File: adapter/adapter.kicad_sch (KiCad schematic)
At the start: 9 parts, among them J10 Ribbon, J11 Ribbon, J12 Ribbon, J9 Ribbon, U1 nice_nano

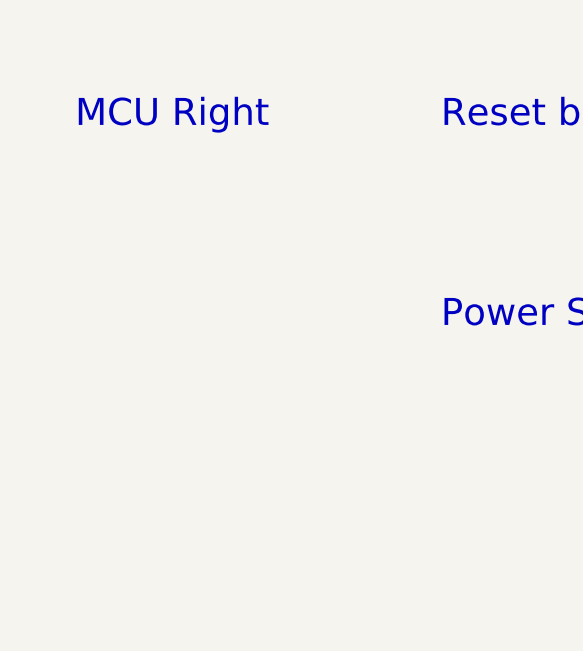
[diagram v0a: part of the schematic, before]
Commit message: Add nice!nano mcu to right side
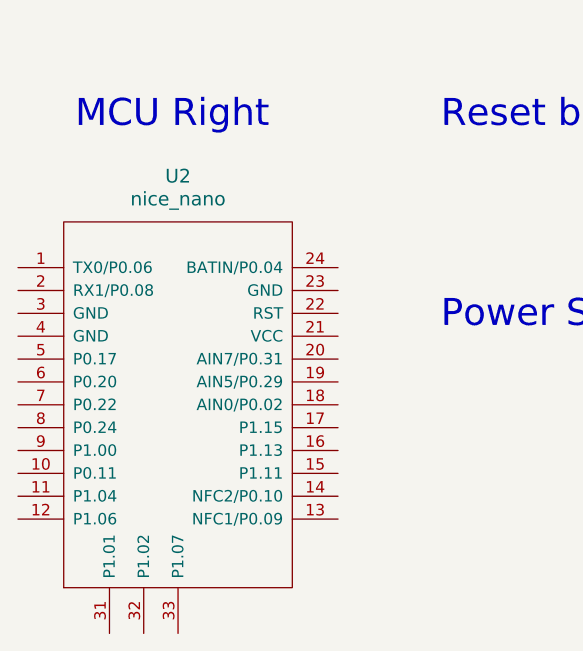
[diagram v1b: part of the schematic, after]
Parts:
- added U2: nice_nano, Library:nice_nano, symbol nice_nano:nice_nano
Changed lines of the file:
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@@
+	)
+	(symbol
+		(lib_id "nice_nano:nice_nano")
+		(at 45.72 129.54 0)
+		(unit 1)
+		(exclude_from_sim no)
+		(in_bom yes)
+		(on_board yes)
+		(dnp no)
+		(fields_autoplaced yes)
+		(property "Reference" "U2"
+			(at 45.72 105.41 0)
+			(effects
+				(font
+					(size 1.524 1.524)
+				)
+			)
+		)
+		(property "Value" "nice_nano"
+			(at 45.72 107.95 0)
+			(effects
+				(font
+					(size 1.524 1.524)
+				)
+			)
+		)
+		(property "Footprint" "Library:nice_nano"
+			(at 72.39 193.04 90)
+			(effects
+				(font
+					(size 1.524 1.524)
+				)
+				(hide yes)
+			)
+		)
+		(property "Datasheet" ""
+			(at 72.39 193.04 90)
+			(effects
+				(font
+					(size 1.524 1.524)
+				)
+				(hide yes)
+			)
+		)
+		(property "Description" ""
+			(at 45.72 129.54 0)
+			(effects
+				(font
+					(size 1.27 1.27)
+				)
+				(hide yes)
+			)
+		)
+		(pin "7"
+		)
+		(pin "1"
+		)
+		(pin "10"
+		)
+		(pin "6"
+		)
+		(pin "5"
+		)
+		(pin "2"
+		)
+		(pin "3"
+		)
+		(pin "4"
+		)
+		(pin "8"
+		)
+		(pin "9"
+		)
+		(pin "12"
+		)
+		(pin "33"
+		)
+		(pin "19"
+		)
+		(pin "16"
+		)
+		(pin "20"
+		)
+		(pin "24"
+		)
+		(pin "15"
+		)
+		(pin "11"
+		)
+		(pin "14"
+		)
+		(pin "17"
+		)
+		(pin "18"
+		)
+		(pin "21"
+		)
+		(pin "23"
+		)
+		(pin "22"
+		)
+		(pin "13"
+		)
+		(pin "31"
+		)
+		(pin "32"
+		)
+		(instances
+			(project ""
+				(path "/e63e39d7-6ac0-4ffd-8aa3-1841a4541b55"
+					(reference "U2")
+					(unit 1)
+				)
+			)
+		)
 	)
 	(symbol

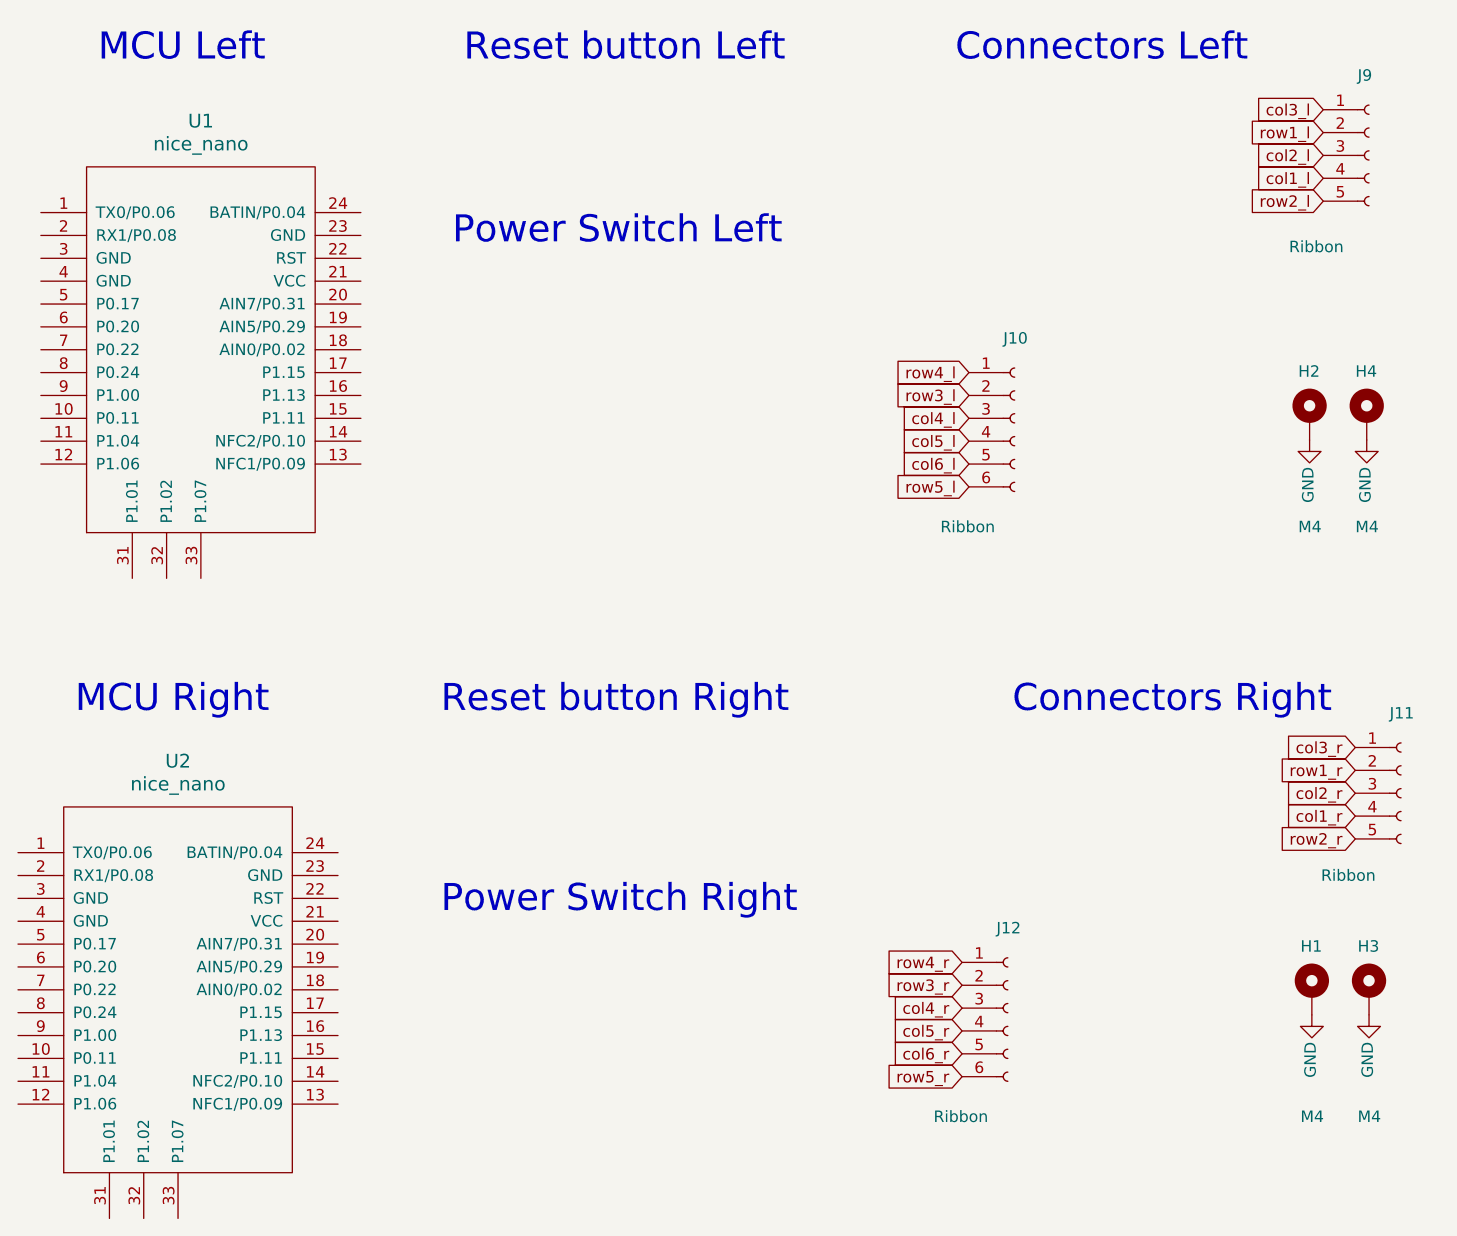
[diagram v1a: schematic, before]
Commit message: Add jst connector and powerswitch
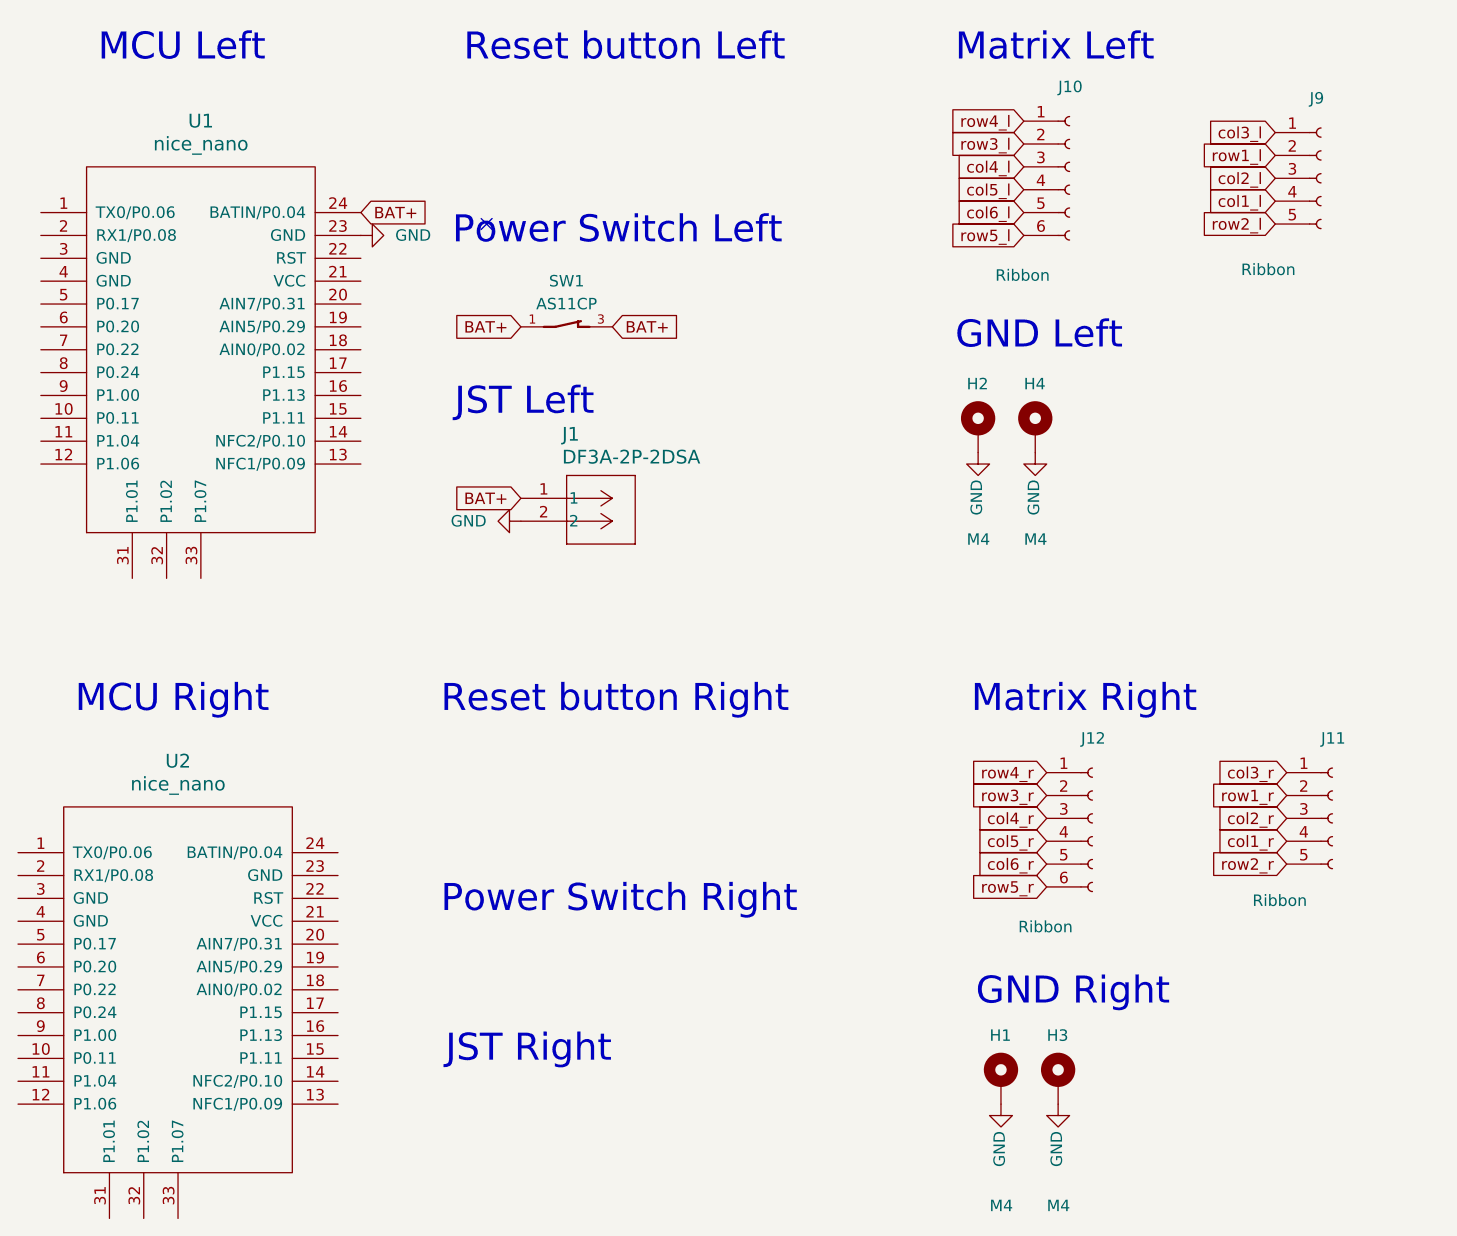
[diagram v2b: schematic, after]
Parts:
- added J1: DF3A-2P-2DSA, Library:DF3A_2P_2DSA, symbol DF3A_2P_2DSA:DF3A-2P-2DSA
- added SW1: AS11CP, Library:SW_AS11CP, symbol AS11CP:AS11CP
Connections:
- net GND: now also U1.23 (GND), J1.2
- net BAT+: now reaches U1.24 (BATIN/P0.04)
- net BAT+: now also J1.1, SW1.1, SW1.3
- no-connect marks 0 -> 1
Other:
- note added: "GND Left"
- note added: "GND Right"
- note added: "JST Left"
- note added: "JST Right"
- note added: "Matrix Left"
- note added: "Matrix Right"
- note removed: "Connectors Left"
- note removed: "Connectors Right"
- moved on the sheet: H1, H2, H3, H4, J10, J11, J12, J9

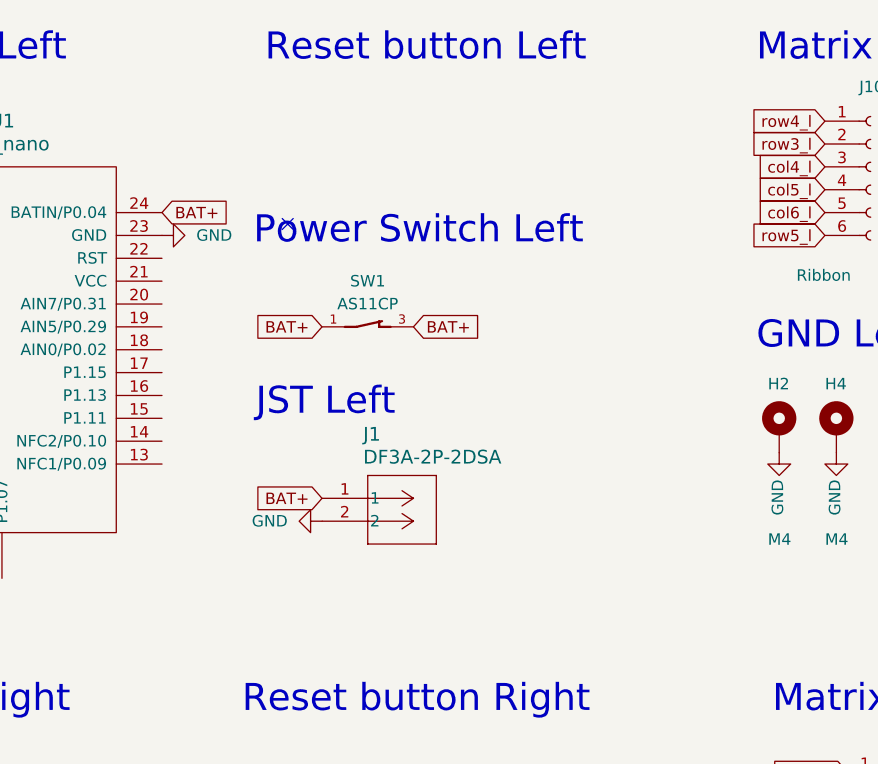
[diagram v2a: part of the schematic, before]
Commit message: Add a resetbutton
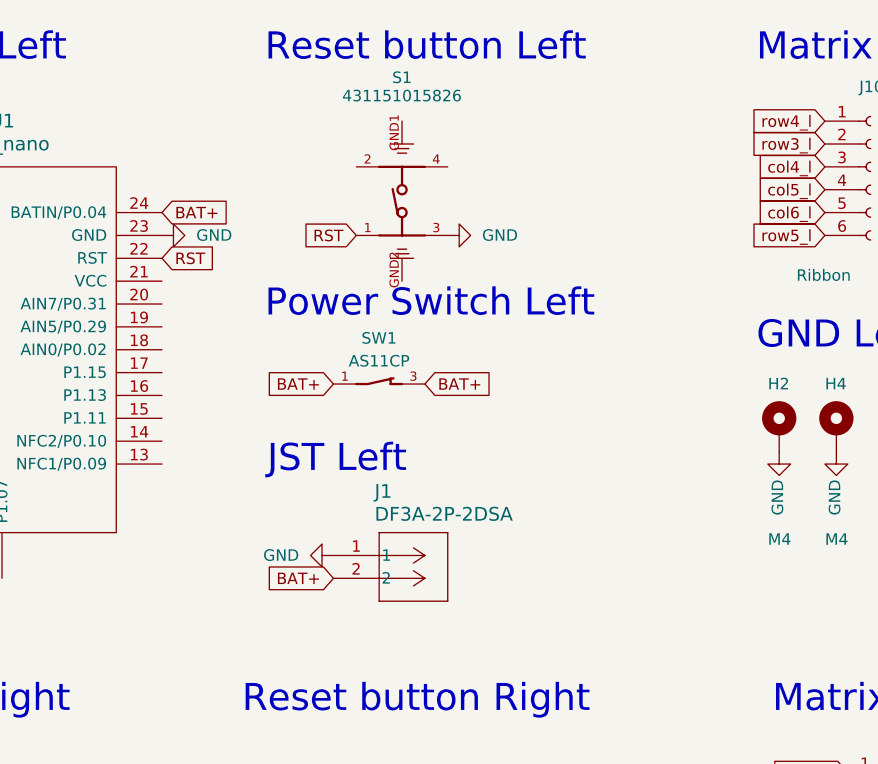
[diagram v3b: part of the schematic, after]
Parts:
- added S1: 431151015826, Library:431151015826, symbol 431151015826:431151015826
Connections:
- net BAT+: now also J1.2; no longer J1.1
- net GND: now also J1.1, S1.3; no longer J1.2
- net RST: now reaches U1.22 (RST)
- net RST: now also S1.1
- no-connect marks 1 -> 0
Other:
- moved on the sheet: J1, SW1

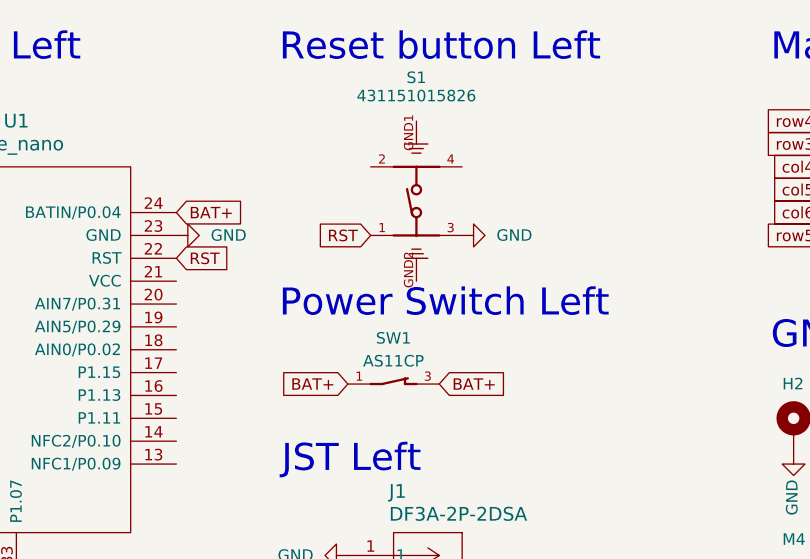
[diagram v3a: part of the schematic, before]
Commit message: Remove power switch
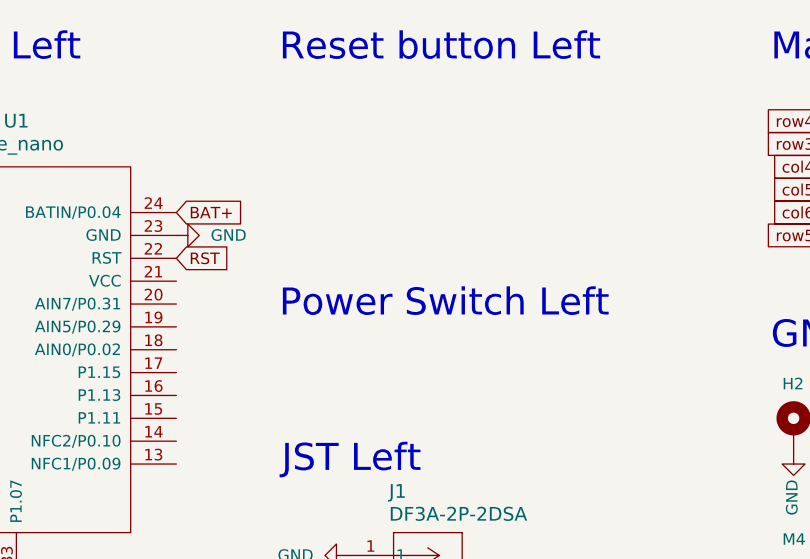
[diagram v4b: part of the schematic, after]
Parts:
- removed S1: 431151015826, Library:431151015826, symbol 431151015826:431151015826
- removed SW1: AS11CP, Library:SW_AS11CP, symbol AS11CP:AS11CP

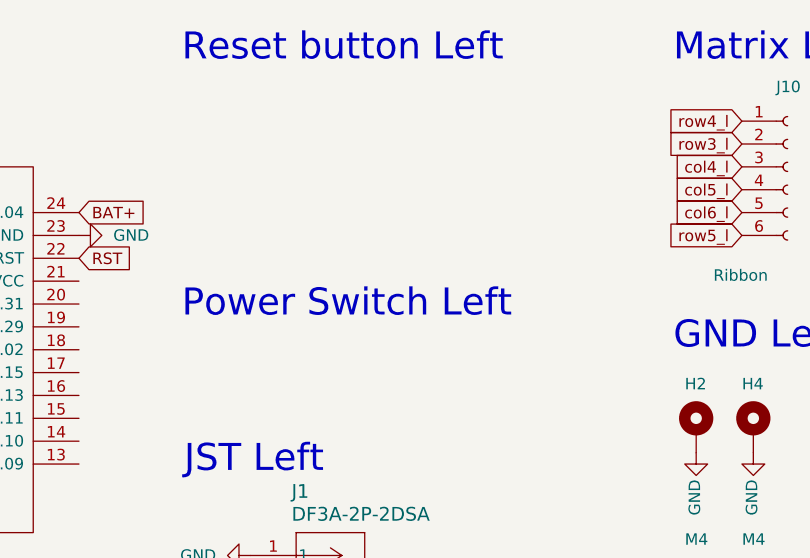
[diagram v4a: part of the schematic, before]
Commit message: Add new power switch and reset button
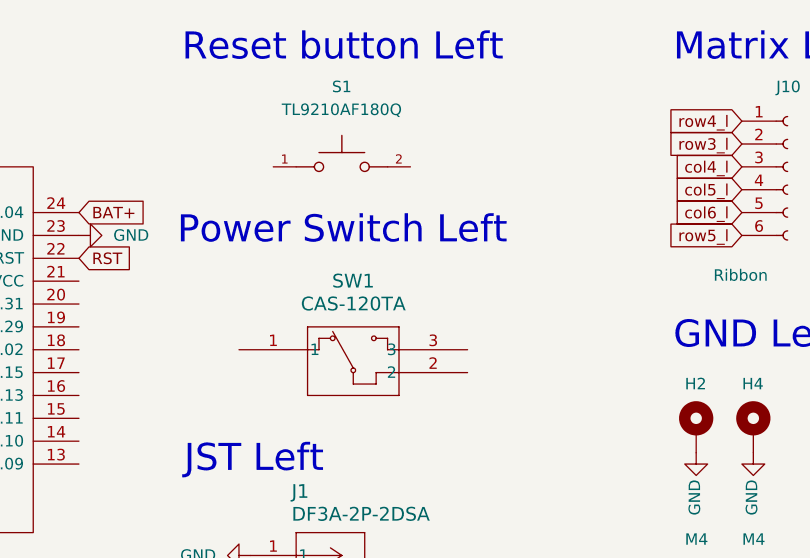
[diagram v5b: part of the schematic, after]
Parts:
- added S1: TL9210AF180Q, Library:SW_TL9210AF180Q, symbol TL9210AF180Q:TL9210AF180Q
- added SW1: CAS-120TA, Library:CAS-120A_NDC, symbol CAS-120TA:CAS-120TA
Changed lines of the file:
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@@
 	(text "Power Switch Left"
 		(exclude_from_sim no)
-		(at 77.47 56.388 0)
+		(at 76.962 48.26 0)
 		(effects
 			(font
@@
 	)
 	(symbol
+		(lib_id "CAS-120TA:CAS-120TA")
+		(at 83.82 59.69 0)
+		(unit 1)
+		(exclude_from_sim no)
+		(in_bom yes)
+		(on_board yes)
+		(dnp no)
+		(fields_autoplaced yes)
+		(property "Reference" "SW1"
+			(at 96.52 52.07 0)
+			(effects
+				(font
+					(size 1.524 1.524)
+				)
+			)
+		)
+		(property "Value" "CAS-120TA"
+			(at 96.52 54.61 0)
+			(effects
+				(font
+					(size 1.524 1.524)
+				)
+			)
+		)
+		(property "Footprint" "Library:CAS-120A_NDC"
+			(at 83.82 59.69 0)
+			(effects
+				(font
+					(size 1.27 1.27)
+					(italic yes)
+				)
+				(hide yes)
+			)
+		)
+		(property "Datasheet" "CAS-120TA"
+			(at 83.82 59.69 0)
+			(effects
+				(font
+					(size 1.27 1.27)
+					(italic yes)
+				)
+				(hide yes)
+			)
+		)
+		(property "Description" ""
+			(at 83.82 59.69 0)
+			(effects
+				(font
+					(size 1.27 1.27)
+				)
+				(hide yes)
+			)
+		)
+		(pin "1"
+		)
+		(pin "3"
+		)
+		(pin "2"
+		)
+		(instances
+			(project ""
+				(path "/e63e39d7-6ac0-4ffd-8aa3-1841a4541b55"
+					(reference "SW1")
+					(unit 1)
+				)
+			)
+		)
+	)
+	(symbol
 		(lib_id "nice_nano:nice_nano")
 		(at 48.26 58.42 0)
@@
 					(unit 1)
 				)
+			)
+		)
+	)
+	(symbol
+		(lib_id "TL9210AF180Q:TL9210AF180Q")
+		(at 95.25 39.37 0)
+		(unit 1)
+		(exclude_from_sim no)
+		(in_bom yes)
+		(on_board yes)
+		(dnp no)
+		(fields_autoplaced yes)
+		(property "Reference" "S1"
+			(at 95.25 30.48 0)
+			(effects
+				(font
+					(size 1.27 1.27)
+				)
+			)
+		)
+		(property "Value" "TL9210AF180Q"
+			(at 95.25 33.02 0)
+			(effects
+				(font
+					(size 1.27 1.27)
+				)
+			)
+		)
+		(property "Footprint" "Library:SW_TL9210AF180Q"
+			(at 95.25 39.37 0)
+			(effects
+				(font
+					(size 1.27 1.27)
+				)
+				(justify bottom)
+				(hide yes)
+			)
+		)
+		(property "Datasheet" ""
+			(at 95.25 39.37 0)
+			(effects
+				(font
+					(size 1.27 1.27)
+				)
+				(hide yes)
+			)
+		)
+		(property "Description" ""
+			(at 95.25 39.37 0)
+			(effects
+				(font
+					(size 1.27 1.27)
+				)
+				(hide yes)
+			)
+		)
+		(property "PARTREV" "E"
+			(at 95.25 39.37 0)
+			(effects
+				(font
+					(size 1.27 1.27)
+				)
+				(justify bottom)
+				(hide yes)
+			)
+		)
+		(property "STANDARD" "Manufacturer Recommendations"
+			(at 95.25 39.37 0)
+			(effects
+				(font
+					(size 1.27 1.27)
+				)
+				(justify bottom)
+				(hide yes)
+			)
+		)
+		(property "MAXIMUM_PACKAGE_HEIGHT" "5.0mm"
+			(at 95.25 39.37 0)
+			(effects
+				(font
+					(size 1.27 1.27)
+				)
+				(justify bottom)
+				(hide yes)
+			)
+		)
+		(property "MANUFACTURER" "E-Switch"
+			(at 95.25 39.37 0)
+			(effects
+				(font
+					(size 1.27 1.27)
+				)
+				(justify bottom)
+				(hide yes)
+			)
+		)
+		(pin "1"
+		)
+		(pin "2"
+		)
+		(instances
+			(project ""
+				(path "/e63e39d7-6ac0-4ffd-8aa3-1841a4541b55"
+					(reference "S1")
+					(unit 1)
+				)
